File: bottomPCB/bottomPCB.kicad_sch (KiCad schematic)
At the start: 36 parts, among them J1 Conn_01x03_Pin, U1 ESP32-WROOM-32, U8 LM1117IMPX-3_3_NOPB, U9 LM1117IMPX-3_3_NOPB

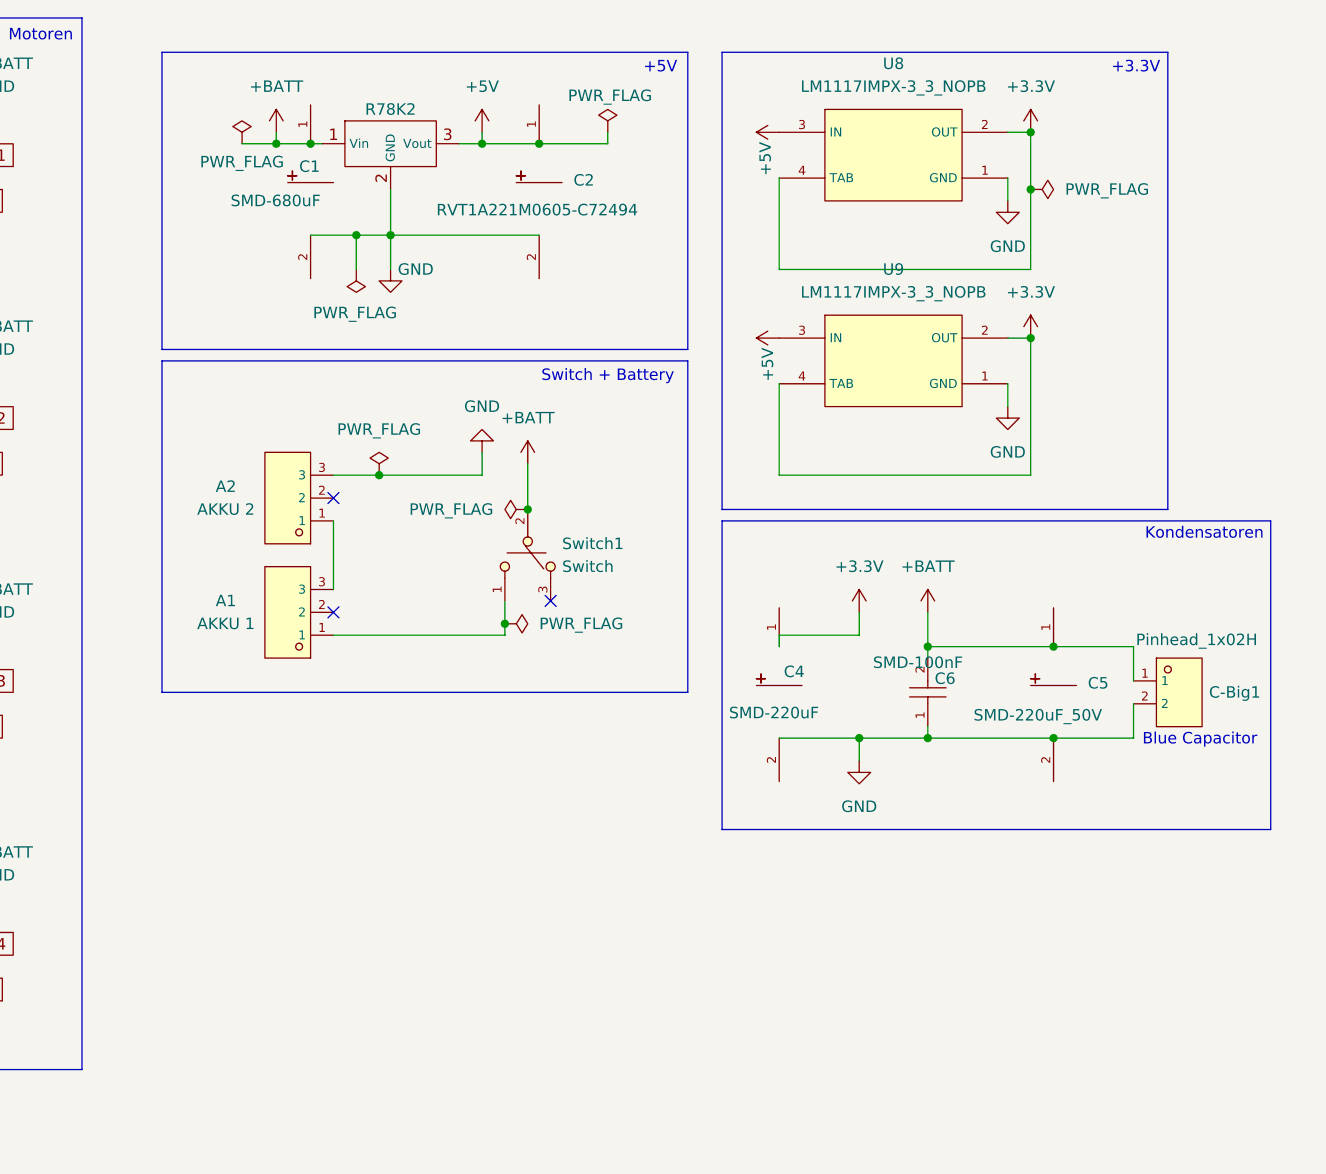
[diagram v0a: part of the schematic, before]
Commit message: replaced 2000mA r78 a 5v Regulator with 4000mA D36V26FX 5v Regulator
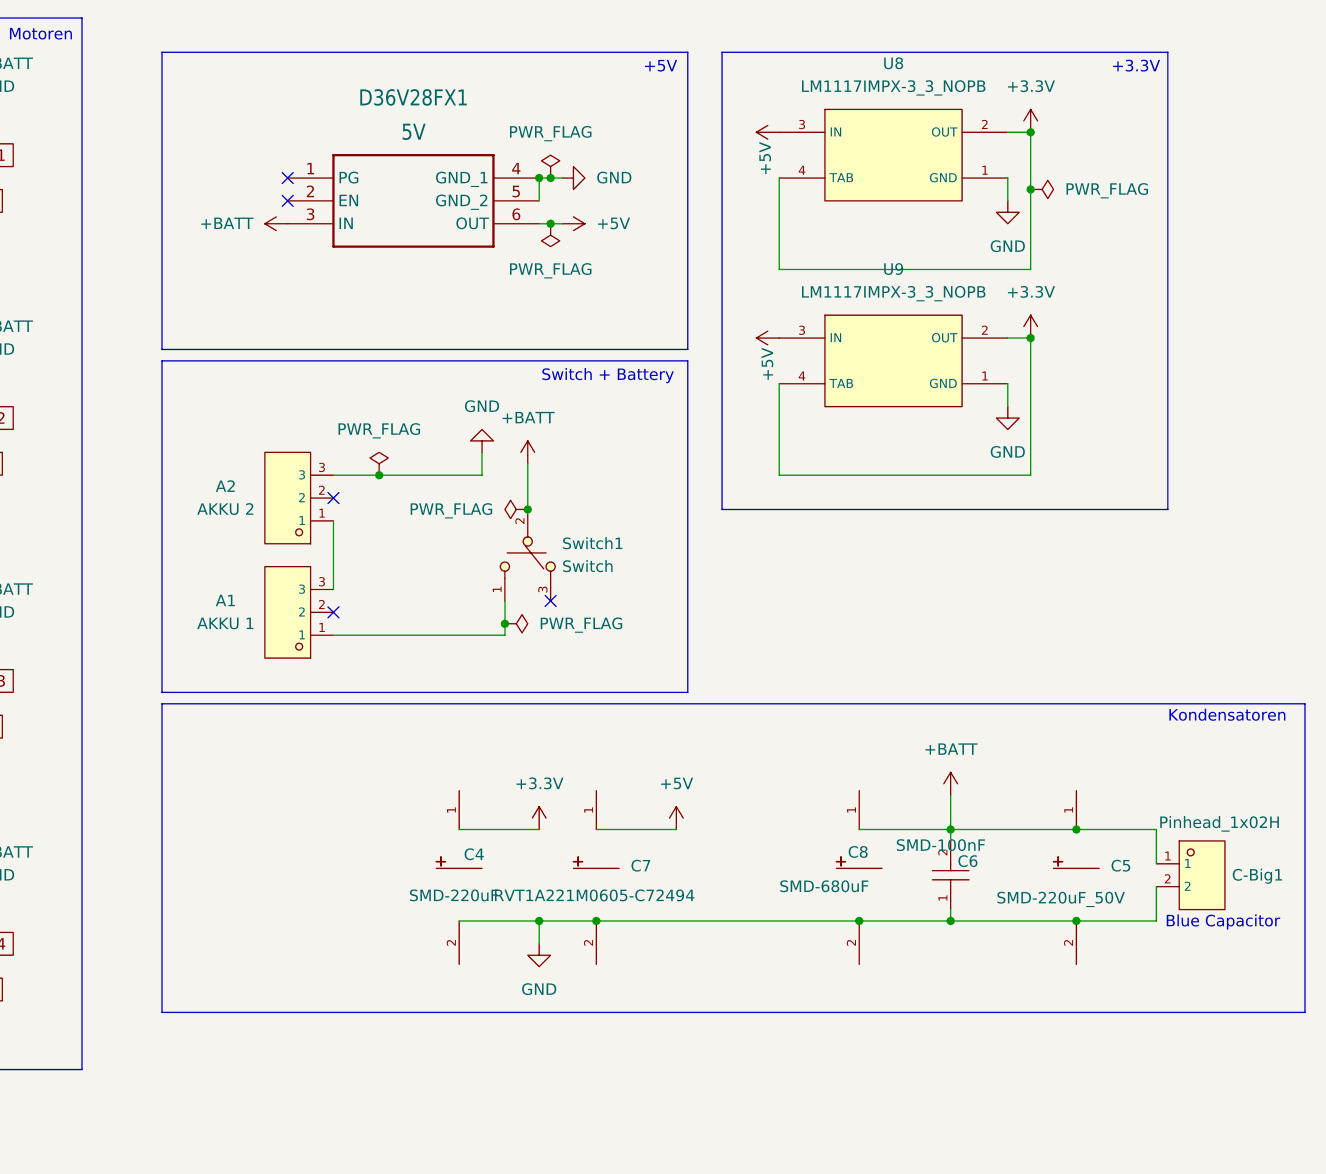
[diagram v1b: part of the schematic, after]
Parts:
- removed C1: SMD-680uF, BohleBots:CAP-SMD_BD10.0-L10.3-W10.3-LS11.3-FD, symbol Bohlebots:SMD-680uF
- removed C2: RVT1A221M0605-C72494, BohleBots:CAP-SMD_BD10.0-L10.3-W10.3-LS11.3-FD, symbol Bohlebots:SMD-220uF_50V
- removed R78K2: ~, BohleBots:R785K, symbol Bohlebots:R78K5
- added C7: RVT1A221M0605-C72494, BohleBots:CAP-SMD_BD10.0-L10.3-W10.3-LS11.3-FD, symbol Bohlebots:SMD-220uF_50V
- added C8: SMD-680uF, BohleBots:CAP-SMD_BD10.0-L10.3-W10.3-LS11.3-FD, symbol Bohlebots:SMD-680uF
- added D36V28FX1: 5V, BohleBots:D36V28FX, symbol bohlebots.lib:D36V28FX
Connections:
- net +5V: now also C7.1, D36V28FX1.6 (OUT)
- net +BATT: now also C8.1, D36V28FX1.3 (IN)
- net GND: now also C7.2, C8.2, D36V28FX1.4 (GND_1), D36V28FX1.5 (GND_2)
- no-connect marks 21 -> 23
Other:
- moved on the sheet: C-Big1, C4, C5, C6

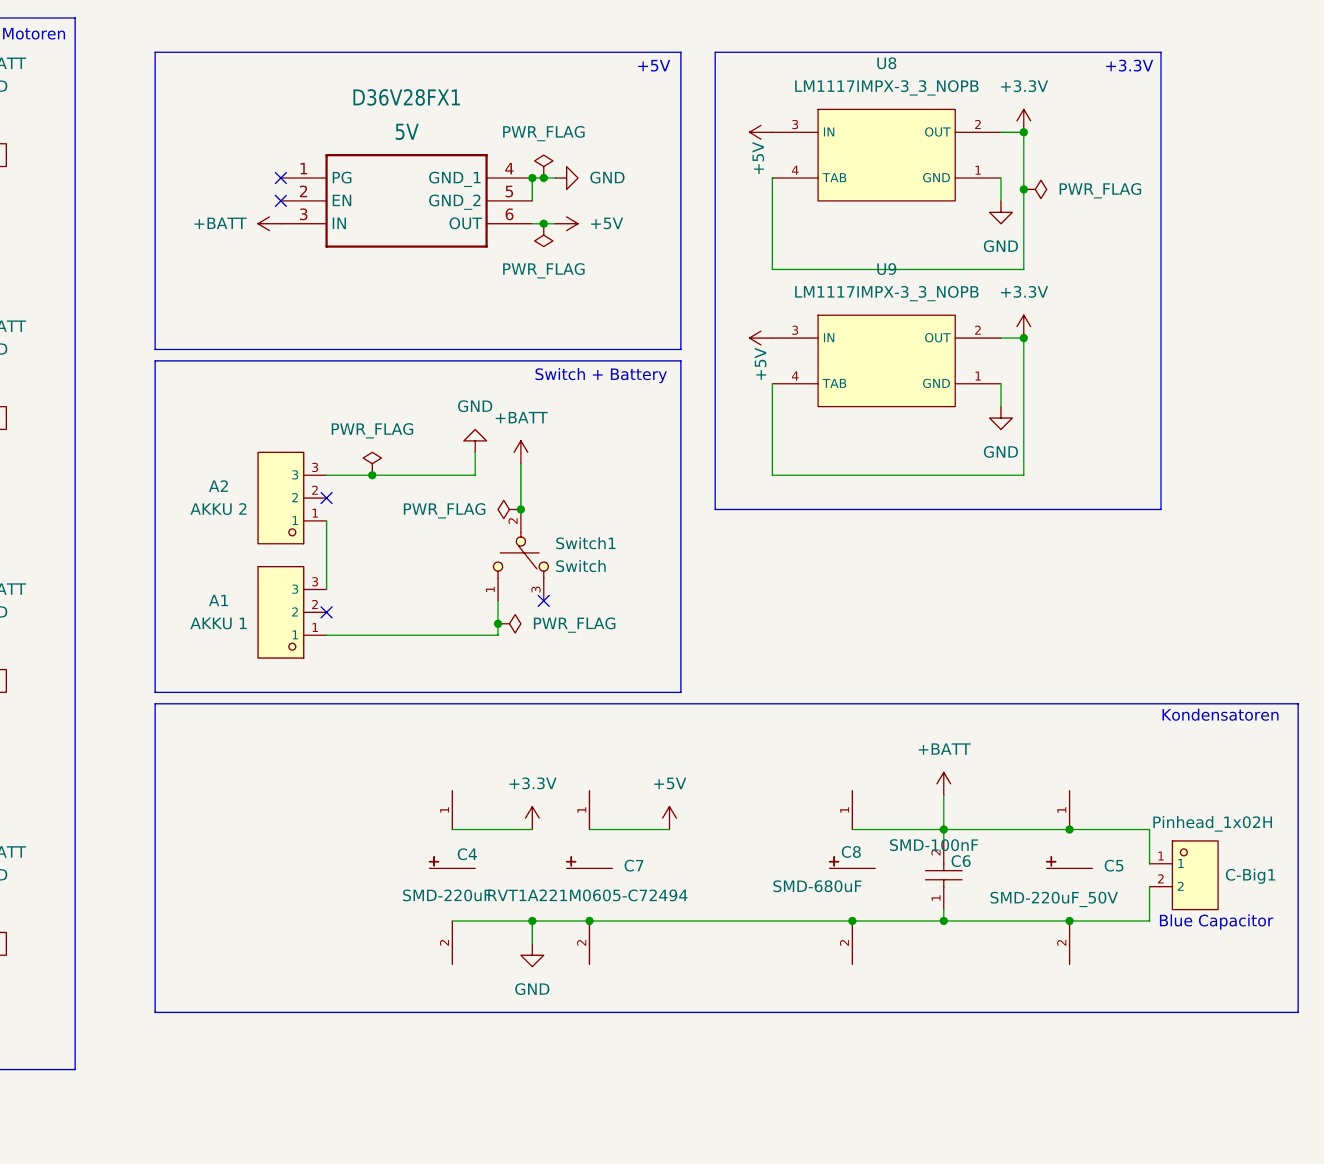
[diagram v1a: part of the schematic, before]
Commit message: added 16V output xt30 connector
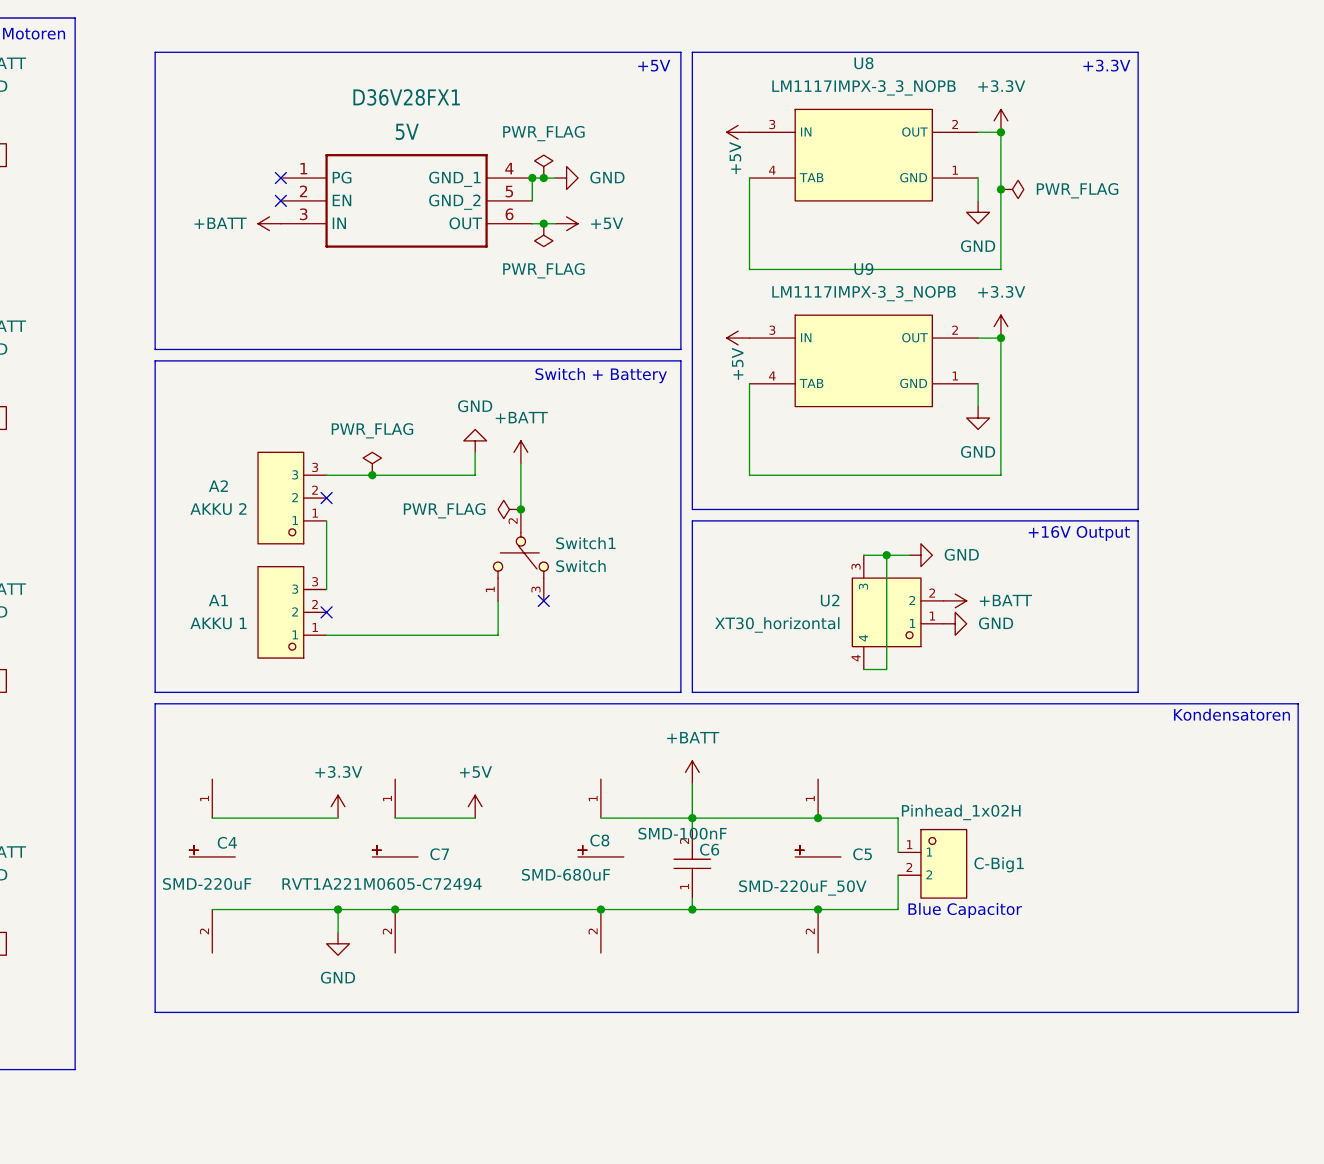
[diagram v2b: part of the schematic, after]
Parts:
- added U2: XT30_horizontal, BohleBots:CONN-TH_XT30PW-M, symbol bohlebots.lib:XT30_horizontal
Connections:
- net +BATT: now also U2.2
- net GND: now also U2.1, U2.3, U2.4
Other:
- note added: "+16V Output"
- moved on the sheet: C-Big1, C4, C5, C6, C7, C8, U8, U9

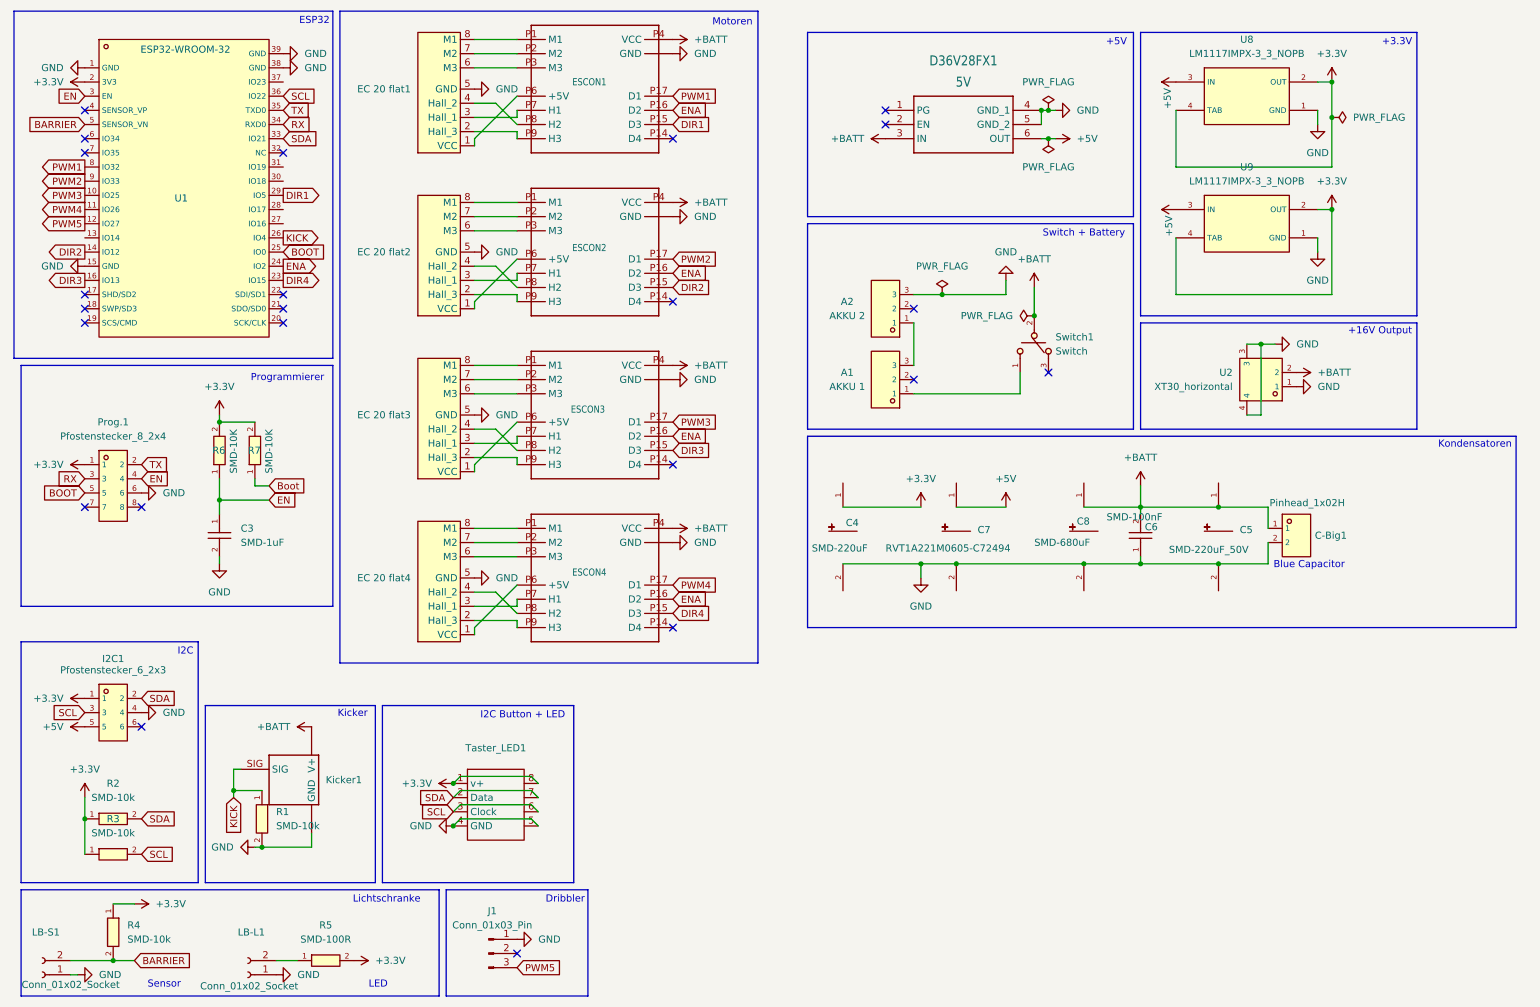
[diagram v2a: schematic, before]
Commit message: added LED
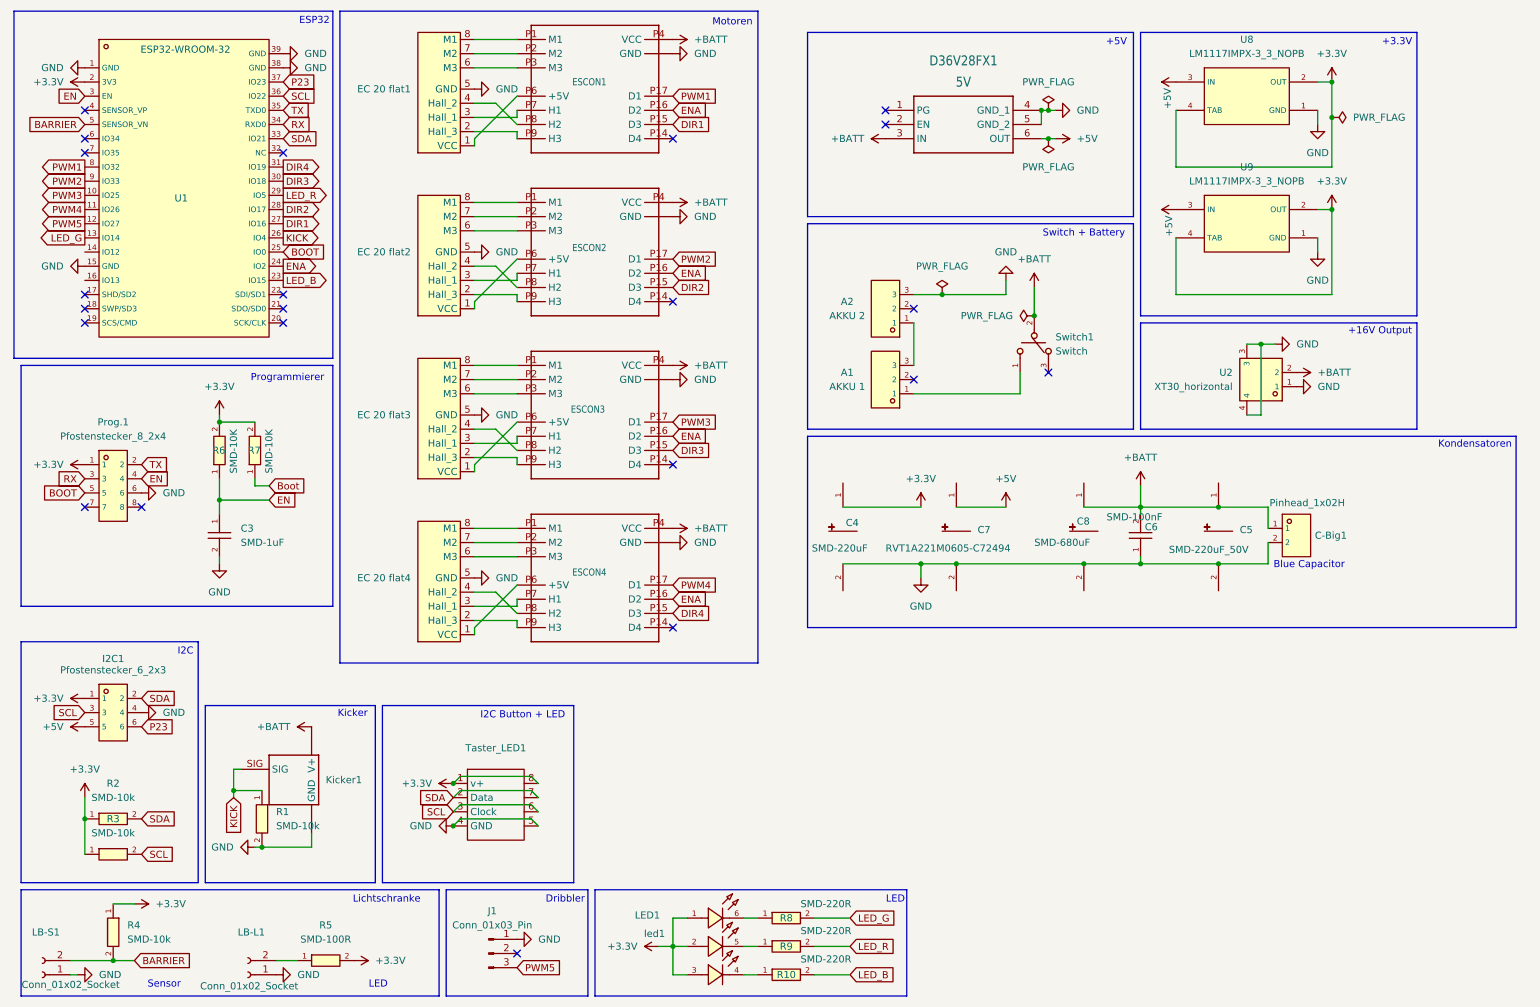
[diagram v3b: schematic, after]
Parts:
- added LED1: led1, BohleBots:LED-SMD_6P-L5.0-W5.0-TL_TC5050RGBF08, symbol Bohlebots:SMD-RGB-LED
- added R10, R8, R9: SMD-220R, BohleBots:R0603, symbol Bohlebots:SMD-220R
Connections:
- net +3.3V: now also LED1.1 (+), LED1.2 (+), LED1.3 (+)
- net DIR1: now also U1.27 (IO16); no longer U1.29 (IO5)
- net DIR2: now also U1.28 (IO17); no longer U1.14 (IO12)
- net DIR3: now also U1.30 (IO18); no longer U1.16 (IO13)
- net DIR4: now also U1.31 (IO19); no longer U1.23 (IO15)
- net P23: now reaches I2C1.6
- net P23: now also U1.37 (IO23)
- net LED_G: now reaches U1.13 (IO14)
- net LED_G: now also R8.2
- new net: LED1.4 (-), R10.1
- new net: LED1.5 (-), R9.1
- new net: LED1.6 (-), R8.1
- new net LED_B: R10.2, U1.23 (IO15)
- new net LED_R: R9.2, U1.29 (IO5)
- no-connect marks 23 -> 22
